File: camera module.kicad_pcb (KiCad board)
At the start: 2 copper layers, 11.4 x 5.7 mm, 156 parts, among them J1 Conn_01x02, J10 Conn_01x04, J11 Conn_01x05, J12 Conn_01x06, J13 Conn_01x02, J15 Conn_02x30_Odd_Even, J17 USB_B_Micro, J18 Conn_01x03, J2 USB_OTG, J3 Conn_01x15, J4 Conn_02x15_Counter_Clockwise, J5 HDMI, J6 Conn_01x15, J7 Conn_01x02, J8 HDMI, J9 HDMI, Q1 EM6K34T2CR, Q10 DMG2305UX, Q11 DMMT5401-7-F, Q12 DMG2305UX, Q2 Q_NMOS_GSD, Q3 Q_NMOS_GSD, Q4 Q_NMOS_GSD, Q5 Q_NMOS_GSD, Q6 Q_NMOS_GSD, Q7 DMMT5401-7-F, Q8 DMG2305UX, Q9 DMMT5401-7-F, SW1 SW_SPST, U1 TPS563208, U10 FSUSB42UMX, U11 USB_A, U2 PAM2306AYPKE, U3 LTC3406ES5-1.2, U4 TS3DDR3812RUAR, U5 TLV70228_SOT23-5, U6 XC6222B181MR-G, U7 LSM6DS3, U8 HDMIULC6-4SC6, U9 AP2331W, Y1 SIT8008AI-73-XXS-33.333333E

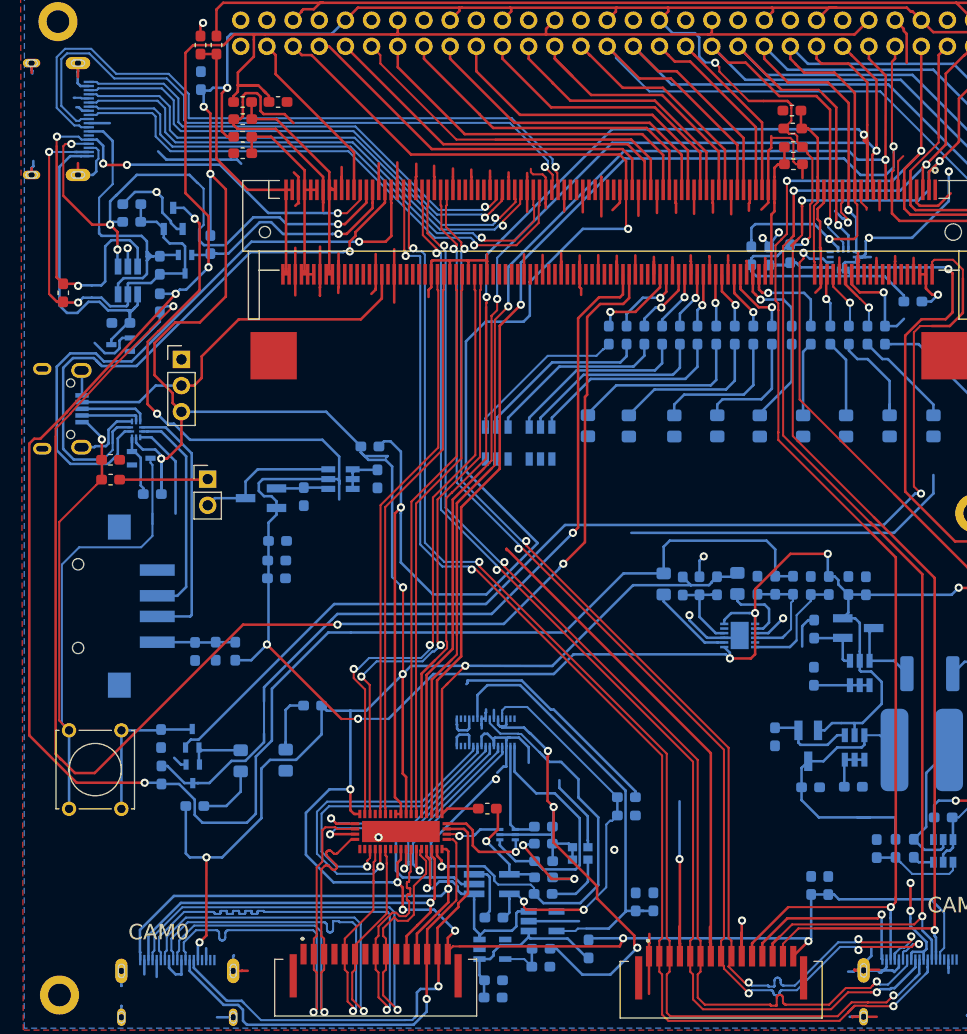
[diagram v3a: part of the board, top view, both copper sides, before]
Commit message: Added some vias to replace plated slots, removed a couple of stray tracks
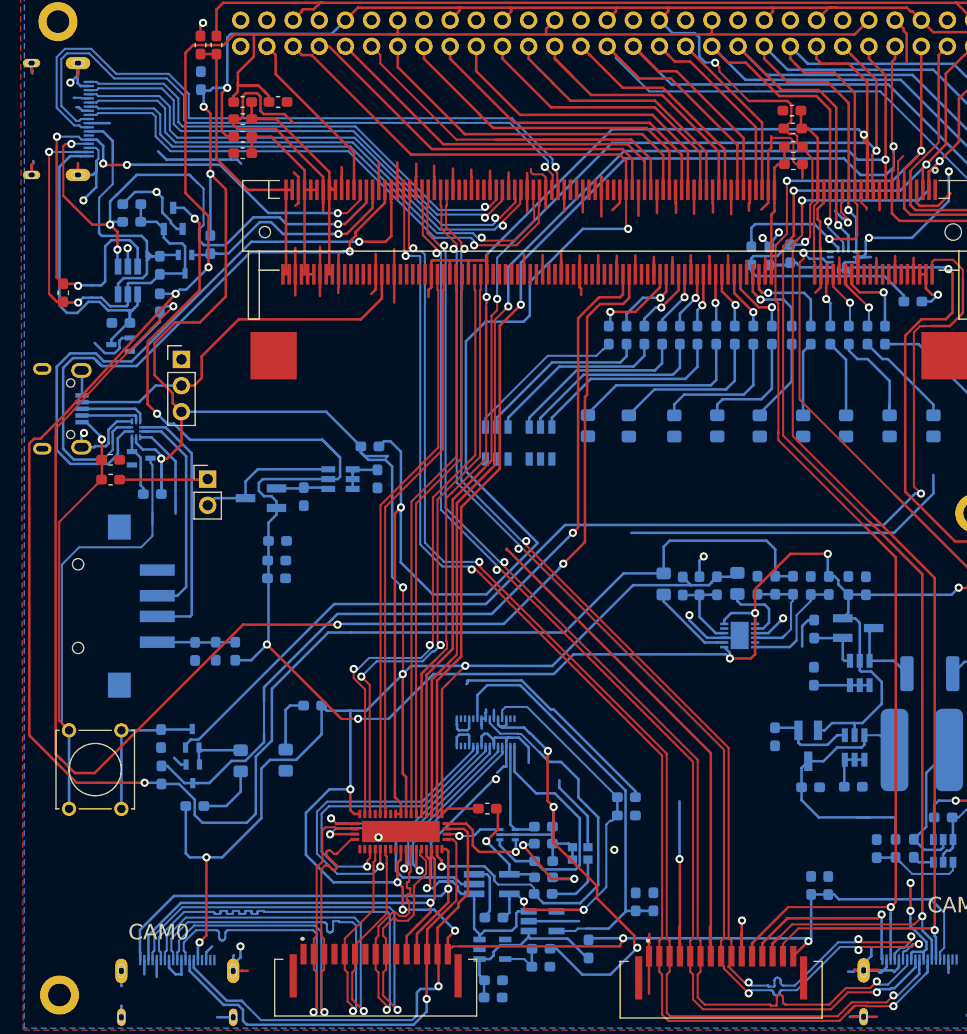
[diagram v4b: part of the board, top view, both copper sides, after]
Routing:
- net GND: track 597.5 -> 609.9 mm, vias 21 -> 25
- net GPIO28: track 9.86 -> 7.73 mm
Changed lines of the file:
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@@
-(kicad_pcb (version 20171130) (host pcbnew "(5.0.1)-4")
+(kicad_pcb (version 20171130) (host pcbnew 5.0.2-bee76a0~70~ubuntu18.04.1)
   (general
     (thickness 1.6)
     (drawings 42)
-    (tracks 3512)
+    (tracks 3528)
     (zones 0)
     (modules 156)
@@
   (segment (start 67.875 129.2) (end 67.95 129.125) (width 0.25) (layer B.Cu) (net 1))
   (segment (start 67.875 130.65) (end 67.875 129.2) (width 0.25) (layer B.Cu) (net 1))
-  (segment (start 65.25 129.6) (end 65.25 128.45) (width 0.25) (layer B.Cu) (net 1))
   (segment (start 62.85 129.6) (end 62.85 131.01) (width 0.25) (layer B.Cu) (net 1))
   (segment (start 62.85 131.01) (end 62.82 130.98) (width 0.25) (layer B.Cu) (net 1))
@@
   (segment (start 54.26 53.405) (end 52.81 53.405) (width 0.25) (layer B.Cu) (net 1))
   (segment (start 54.585001 53.079999) (end 54.26 53.405) (width 0.25) (layer B.Cu) (net 1))
-  (segment (start 48.31 52.73) (end 48.48 52.56) (width 0.25) (layer B.Cu) (net 1))
-  (segment (start 48.31 53.405) (end 48.31 52.73) (width 0.25) (layer B.Cu) (net 1))
-  (segment (start 48.48 52.56) (end 48.48 52.05) (width 0.25) (layer B.Cu) (net 1))
   (segment (start 48.31 43.23) (end 48.38 43.3) (width 0.25) (layer B.Cu) (net 1))
   (segment (start 48.31 42.555) (end 48.31 43.23) (width 0.25) (layer B.Cu) (net 1))
@@
   (segment (start 135.898841 117.829946) (end 135.823841 117.904946) (width 0.25) (layer B.Cu) (net 1))
   (segment (start 135.898841 115.754946) (end 135.898841 117.829946) (width 0.25) (layer B.Cu) (net 1))
+  (segment (start 48.31 52.445) (end 48.48 52.275) (width 0.25) (layer B.Cu) (net 1))
+  (segment (start 48.31 53.405) (end 48.31 52.445) (width 0.25) (layer B.Cu) (net 1))
+  (segment (start 48.48 52.275) (end 48.48 52.05) (width 0.25) (layer B.Cu) (net 1))
+  (segment (start 48.31 52.73) (end 48.3 52.72) (width 0.25) (layer F.Cu) (net 1))
+  (segment (start 48.31 53.405) (end 48.31 52.73) (width 0.25) (layer F.Cu) (net 1))
+  (segment (start 48.3 52.72) (end 48.3 52.45) (width 0.25) (layer F.Cu) (net 1))
+  (segment (start 48.3 52.45) (end 48.475 52.275) (width 0.25) (layer F.Cu) (net 1))
+  (segment (start 68.58 129.345) (end 68.58 128.27) (width 0.25) (layer B.Cu) (net 1))
+  (segment (start 67.875 130.65) (end 67.875 130.05) (width 0.25) (layer B.Cu) (net 1))
+  (via (at 68.58 128.27) (size 0.8) (drill 0.4) (layers F.Cu B.Cu) (net 1))
+  (segment (start 67.875 130.05) (end 68.58 129.345) (width 0.25) (layer B.Cu) (net 1))
+  (segment (start 65.25 128.85) (end 65.83 128.27) (width 0.25) (layer B.Cu) (net 1))
+  (segment (start 65.25 129.6) (end 65.25 128.85) (width 0.25) (layer B.Cu) (net 1))
+  (segment (start 54.585001 52.05) (end 54.585001 54.585001) (width 0.25) (layer B.Cu) (net 1))
+  (via (at 53.34 55.88) (size 0.8) (drill 0.4) (layers F.Cu B.Cu) (net 1))
+  (segment (start 54.585001 54.585001) (end 53.34 55.830002) (width 0.25) (layer B.Cu) (net 1))
+  (segment (start 53.34 55.830002) (end 53.34 55.88) (width 0.25) (layer B.Cu) (net 1))
+  (via (at 52.07 44.45) (size 0.8) (drill 0.4) (layers F.Cu B.Cu) (net 1))
+  (segment (start 52.81 42.555) (end 52.81 43.71) (width 0.25) (layer B.Cu) (net 1))
+  (segment (start 52.81 43.71) (end 52.07 44.45) (width 0.25) (layer B.Cu) (net 1))
+  (via (at 53.4 78.45) (size 0.8) (drill 0.4) (layers F.Cu B.Cu) (net 1))
+  (segment (start 53.15 79.825) (end 53.15 78.7) (width 0.25) (layer B.Cu) (net 1))
+  (segment (start 53.15 78.7) (end 53.4 78.45) (width 0.25) (layer B.Cu) (net 1))
   (segment (start 74.534999 37.535001) (end 74.534999 37.465001) (width 0.25) (layer F.Cu) (net 2))
   (segment (start 73.685 38.385) (end 74.534999 37.535001) (width 0.25) (layer F.Cu) (net 2))
@@
   (segment (start 116.078 99.778) (end 115.525 99.225) (width 0.25) (layer B.Cu) (net 2))
   (segment (start 116.078 100.33) (end 116.078 99.778) (width 0.25) (layer B.Cu) (net 2))
-  (segment (start 77.1 82.925) (end 78.025 82.925) (width 0.25) (layer B.Cu) (net 2))
-  (segment (start 78.025 82.925) (end 78.16 83.06) (width 0.25) (layer B.Cu) (net 2))
-  (via (at 64.14 57.65) (size 0.8) (drill 0.4) (layers F.Cu B.Cu) (net 2))
-  (segment (start 62.05 56.6) (end 63.09 56.6) (width 0.25) (layer B.Cu) (net 2))
-  (segment (start 63.09 56.6) (end 64.14 57.65) (width 0.25) (layer B.Cu) (net 2))
-  (segment (start 64.14 57.65) (end 64.61 58.12) (width 0.25) (layer F.Cu) (net 2))
-  (segment (start 64.61 58.12) (end 64.61 64.6) (width 0.25) (layer F.Cu) (net 2))
-  (via (at 60.49 76.58) (size 0.8) (drill 0.4) (layers F.Cu B.Cu) (net 2))
-  (segment (start 59.56 69.915012) (end 59.56 75.65) (width 0.25) (layer F.Cu) (net 2))
-  (segment (start 59.56 75.65) (end 60.49 76.58) (width 0.25) (layer F.Cu) (net 2))
-  (segment (start 61.45999 77.54999) (end 62.11999 77.54999) (width 0.25) (layer B.Cu) (net 2))
-  (segment (start 60.49 76.58) (end 61.45999 77.54999) (width 0.25) (layer B.Cu) (net 2))
-  (segment (start 62.11999 77.54999) (end 63.68 79.11) (width 0.25) (layer B.Cu) (net 2))
-  (segment (start 63.68 79.11) (end 76.53 79.11) (width 0.25) (layer B.Cu) (net 2))
-  (segment (start 78.16 80.74) (end 78.16 83.38) (width 0.25) (layer B.Cu) (net 2))
-  (segment (start 76.53 79.11) (end 78.16 80.74) (width 0.25) (layer B.Cu) (net 2))
-  (segment (start 78.16 83.06) (end 78.16 83.38) (width 0.25) (layer B.Cu) (net 2))
-  (segment (start 78.16 83.38) (end 78.16 84.9) (width 0.25) (layer B.Cu) (net 2))
   (segment (start 115.678001 99.930001) (end 100.899999 99.930001) (width 0.25) (layer B.Cu) (net 2))
   (segment (start 116.078 100.33) (end 115.678001 99.930001) (width 0.25) (layer B.Cu) (net 2))
@@
   (segment (start 137.59 94.15) (end 129.275 94.15) (width 0.25) (layer B.Cu) (net 2))
   (segment (start 138.28 93.46) (end 137.59 94.15) (width 0.25) (layer B.Cu) (net 2))
-  (segment (start 60.64 68.57) (end 60.59 68.57) (width 0.2) (layer F.Cu) (net 2))
-  (segment (start 64.61 64.6) (end 60.64 68.57) (width 0.25) (layer F.Cu) (net 2))
-  (segment (start 59.56 69.6) (end 59.56 69.915012) (width 0.2) (layer F.Cu) (net 2))
-  (segment (start 60.59 68.57) (end 59.56 69.6) (width 0.2) (layer F.Cu) (net 2))
   (via (at 79.99 106.19) (size 0.8) (drill 0.4) (layers F.Cu B.Cu) (net 2))
   (segment (start 78.375 106.2) (end 79.98 106.2) (width 0.2) (layer F.Cu) (net 2))
@@
   (segment (start 126.88 106.599787) (end 128.12 106.599787) (width 0.25) (layer B.Cu) (net 2))
   (segment (start 128.12 106.599787) (end 128.940213 106.599787) (width 0.25) (layer B.Cu) (net 2))
+  (via (at 64.14 57.65) (size 0.8) (drill 0.4) (layers F.Cu B.Cu) (net 2))
+  (via (at 60.49 76.58) (size 0.8) (drill 0.4) (layers F.Cu B.Cu) (net 2))
+  (segment (start 59.56 69.6) (end 59.56 69.915012) (width 0.2) (layer F.Cu) (net 2))
+  (segment (start 64.61 64.6) (end 60.64 68.57) (width 0.25) (layer F.Cu) (net 2))
+  (segment (start 60.64 68.57) (end 60.59 68.57) (width 0.2) (layer F.Cu) (net 2))
+  (segment (start 60.59 68.57) (end 59.56 69.6) (width 0.2) (layer F.Cu) (net 2))
+  (segment (start 63.09 56.6) (end 64.14 57.65) (width 0.25) (layer B.Cu) (net 2))
+  (segment (start 59.56 75.65) (end 60.49 76.58) (width 0.25) (layer F.Cu) (net 2))
+  (segment (start 59.56 69.915012) (end 59.56 75.65) (width 0.25) (layer F.Cu) (net 2))
+  (segment (start 64.61 58.12) (end 64.61 64.6) (width 0.25) (layer F.Cu) (net 2))
+  (segment (start 64.14 57.65) (end 64.61 58.12) (width 0.25) (layer F.Cu) (net 2))
+  (segment (start 77.1 82.925) (end 78.025 82.925) (width 0.25) (layer B.Cu) (net 2))
+  (segment (start 76.53 79.11) (end 78.16 80.74) (width 0.25) (layer B.Cu) (net 2))
+  (segment (start 60.49 76.58) (end 61.45999 77.54999) (width 0.25) (layer B.Cu) (net 2))
+  (segment (start 62.05 56.6) (end 63.09 56.6) (width 0.25) (layer B.Cu) (net 2))
+  (segment (start 63.68 79.11) (end 76.53 79.11) (width 0.25) (layer B.Cu) (net 2))
+  (segment (start 62.11999 77.54999) (end 63.68 79.11) (width 0.25) (layer B.Cu) (net 2))
+  (segment (start 61.45999 77.54999) (end 62.11999 77.54999) (width 0.25) (layer B.Cu) (net 2))
+  (segment (start 78.025 82.925) (end 78.25 82.7) (width 0.25) (layer B.Cu) (net 2))
+  (segment (start 78.25 80.83) (end 76.53 79.11) (width 0.25) (layer B.Cu) (net 2))
+  (segment (start 78.25 82.7) (end 78.25 80.83) (width 0.25) (layer B.Cu) (net 2))
   (segment (start 123.925 94.125) (end 125.675 94.125) (width 0.25) (layer B.Cu) (net 3))
   (segment (start 123.925 94.125) (end 123.925 94.755) (width 0.25) (layer B.Cu) (net 3))
@@
   (segment (start 128.669998 64.8) (end 127.9 64.030002) (width 0.25) (layer F.Cu) (net 134))
   (segment (start 131 64.8) (end 128.669998 64.8) (width 0.25) (layer F.Cu) (net 134))
-  (segment (start 132.265 68.075) (end 132.97 67.37) (width 0.25) (layer B.Cu) (net 134))
-  (segment (start 131.125 68.075) (end 132.265 68.075) (width 0.25) (layer B.Cu) (net 134))
   (segment (start 53.2 76.1) (end 58.375 76.1) (width 0.25) (layer B.Cu) (net 135))
   (segment (start 58.85 76.575) (end 58.85 77.3315) (width 0.25) (layer B.Cu) (net 135))

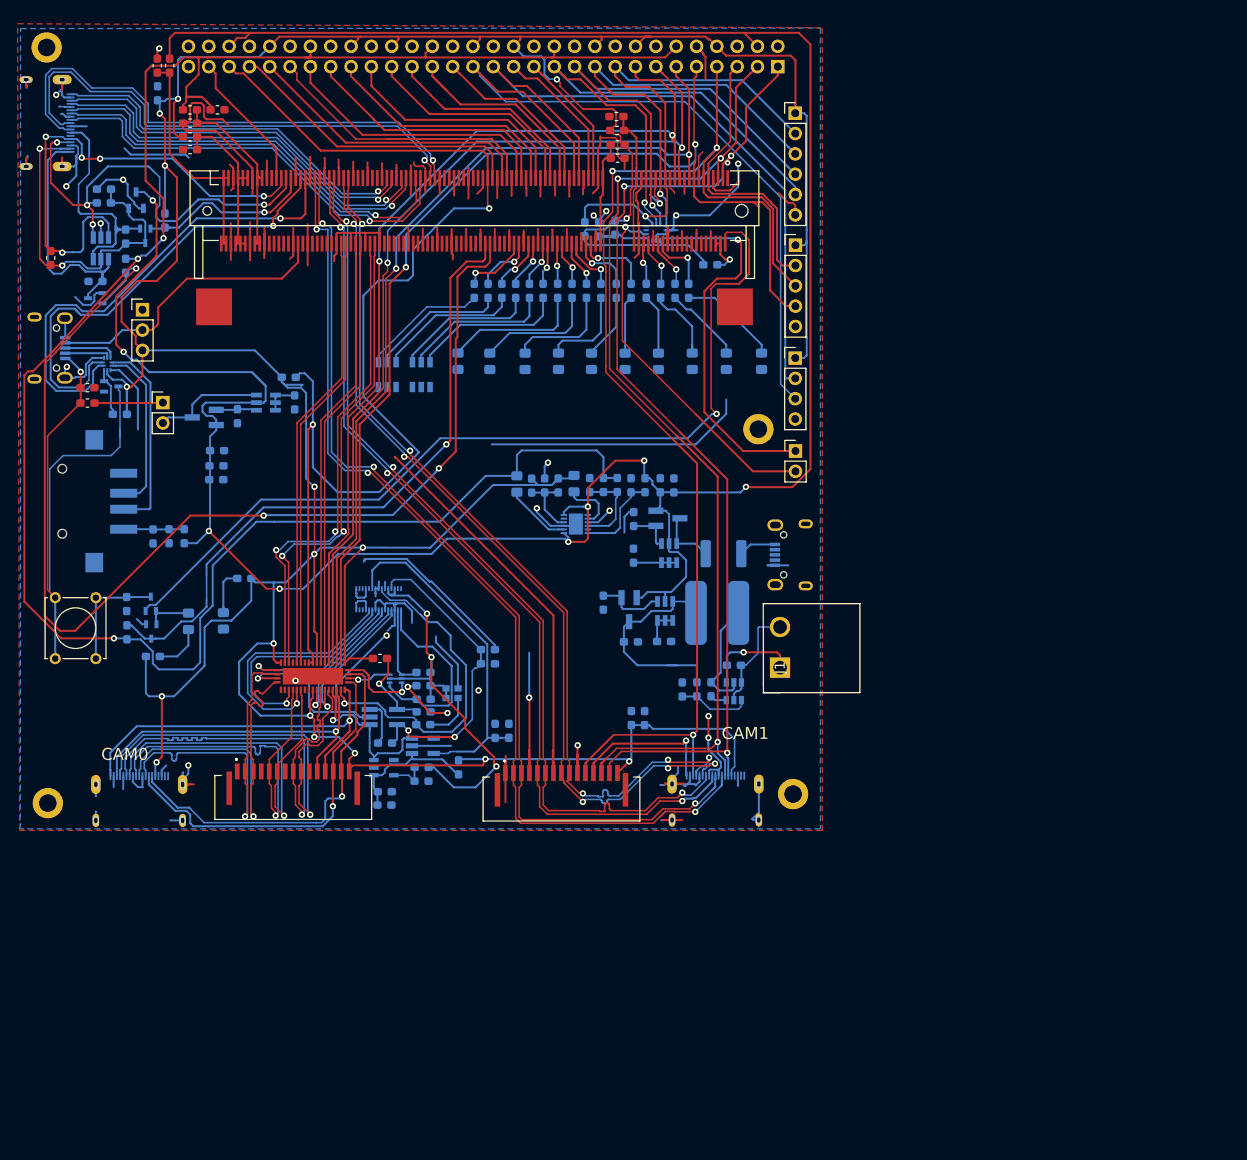
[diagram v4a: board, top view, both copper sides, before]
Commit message: Added missing outline on edgecuts layer(!)
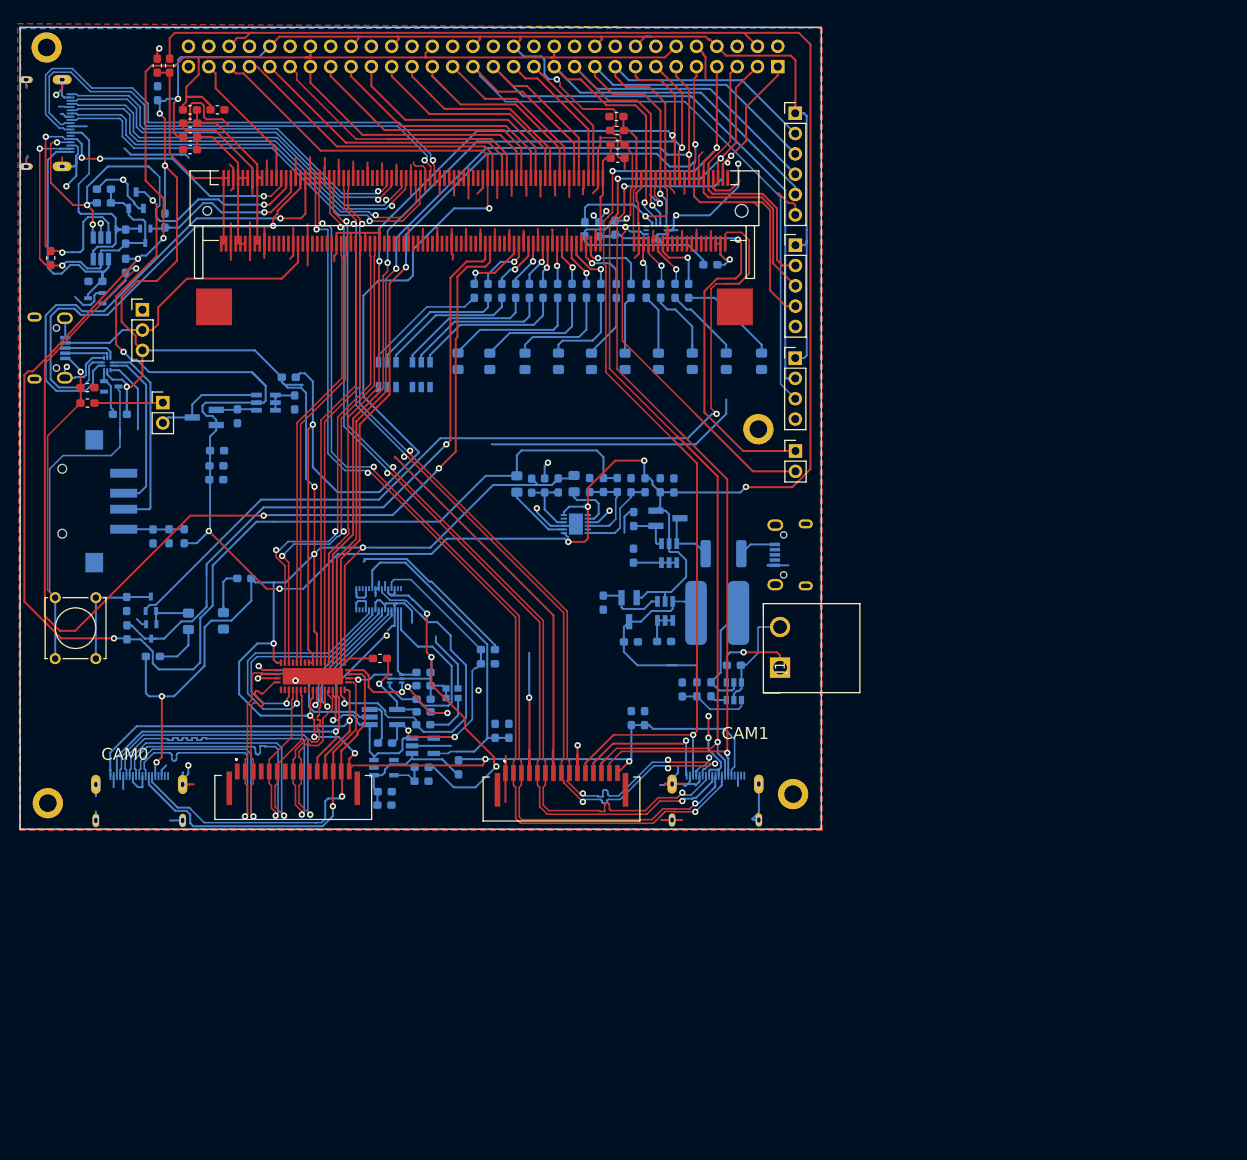
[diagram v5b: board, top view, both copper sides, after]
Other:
- board size 11.4 x 5.7 mm -> 100.1 x 100.2 mm
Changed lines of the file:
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@@
   (general
     (thickness 1.6)
-    (drawings 42)
+    (drawings 47)
     (tracks 3528)
     (zones 0)
@@
   (page A4)
   (layers
-    (0 F.Cu signal)
+    (0 F.Cu signal hide)
     (31 B.Cu signal)
-    (32 B.Adhes user)
-    (33 F.Adhes user)
-    (34 B.Paste user)
-    (35 F.Paste user)
-    (36 B.SilkS user)
-    (37 F.SilkS user)
-    (38 B.Mask user)
-    (39 F.Mask user)
-    (40 Dwgs.User user)
-    (41 Cmts.User user)
-    (42 Eco1.User user)
-    (43 Eco2.User user)
+    (32 B.Adhes user hide)
+    (33 F.Adhes user hide)
+    (34 B.Paste user hide)
+    (35 F.Paste user hide)
+    (36 B.SilkS user hide)
+    (37 F.SilkS user hide)
+    (38 B.Mask user hide)
+    (39 F.Mask user hide)
+    (40 Dwgs.User user hide)
+    (41 Cmts.User user hide)
+    (42 Eco1.User user hide)
+    (43 Eco2.User user hide)
     (44 Edge.Cuts user)
-    (45 Margin user)
-    (46 B.CrtYd user)
-    (47 F.CrtYd user)
-    (48 B.Fab user)
-    (49 F.Fab user)
+    (45 Margin user hide)
+    (46 B.CrtYd user hide)
+    (47 F.CrtYd user hide)
+    (48 B.Fab user hide)
+    (49 F.Fab user hide)
   )
   (setup
@@
     )
   )
+  (gr_line (start 147.7 136.25) (end 147.7 36) (layer Edge.Cuts) (width 0.15))
+  (gr_line (start 47.55 36) (end 47.55 36.3) (layer Edge.Cuts) (width 0.15))
+  (gr_line (start 147.7 36) (end 47.55 36) (layer Edge.Cuts) (width 0.15))
+  (gr_line (start 47.55 136.25) (end 47.55 36.1) (layer Edge.Cuts) (width 0.2))
+  (gr_line (start 147.7 136.25) (end 47.55 136.25) (layer Edge.Cuts) (width 0.2))
   (gr_text "41\n42\n43" (at 93.2 83.98 270) (layer B.SilkS)
     (effects (font (size 0.5 0.5) (thickness 0.125)) (justify mirror))
